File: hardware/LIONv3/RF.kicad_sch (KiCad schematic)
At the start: 17 parts, among them U5 E80-900M2213S, U6 INA226AIDGSR, U7 XL-1608UBC-04, U8 W25Q16JVSSIQTR

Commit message: feat(hardware): annotate schematic with I2C addresses
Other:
- note added: "Table 6-2 (Page 18)"
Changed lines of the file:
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@@
+		)
+	)
+	(text "Table 6-2 (Page 18)"
+		(exclude_from_sim no)
+		(at 143.51 69.85 0)
+		(effects
+			(font
+				(size 1.27 1.27)
+			)
 		)
 	)
@@
 		)
 	)
+	(table
+		(column_count 5)
+		(border
+			(external no)
+			(header yes)
+			(stroke
+				(width 0)
+				(type solid)
+			)
+		)
+		(separators
+			(rows no)
+			(cols no)
+		)
+		(column_widths 5.08 5.08 10.16 6.35 5.08)
+		(row_heights 2.54 2.54)
+		(cells
+			(table_cell "A0"
+				(exclude_from_sim no)
+				(at 127 71.12 0)
+				(size 5.08 2.54)
+				(margins 0.9525 0.9525 0.9525 0.9525)
+				(span 1 1)
+				(fill
+					(type none)
+				)
+				(effects
+					(font
+						(size 1.27 1.27)
+					)
+					(justify left top)
+				)
+			)
+			(table_cell "A1"
+				(exclude_from_sim no)
+				(at 132.08 71.12 0)
+				(size 5.08 2.54)
+				(margins 0.9525 0.9525 0.9525 0.9525)
+				(span 1 1)
+				(fill
+					(type none)
+				)
+				(effects
+					(font
+						(size 1.27 1.27)
+					)
+					(justify left top)
+				)
+			)
+			(table_cell "Binary"
+				(exclude_from_sim no)
+				(at 137.16 71.12 0)
+				(size 10.16 2.54)
+				(margins 0.9525 0.9525 0.9525 0.9525)
+				(span 1 1)
+				(fill
+					(type none)
+				)
+				(effects
+					(font
+						(size 1.27 1.27)
+					)
+					(justify left top)
+				)
+			)
+			(table_cell "Hex"
+				(exclude_from_sim no)
+				(at 147.32 71.12 0)
+				(size 6.35 2.54)
+				(margins 0.9525 0.9525 0.9525 0.9525)
+				(span 1 1)
+				(fill
+					(type none)
+				)
+				(effects
+					(font
+						(size 1.27 1.27)
+					)
+					(justify left top)
+				)
+			)
+			(table_cell "Dec"
+				(exclude_from_sim no)
+				(at 153.67 71.12 0)
+				(size 5.08 2.54)
+				(margins 0.9525 0.9525 0.9525 0.9525)
+				(span 1 1)
+				(fill
+					(type none)
+				)
+				(effects
+					(font
+						(size 1.27 1.27)
+					)
+					(justify left top)
+				)
+			)
+			(table_cell "GND"
+				(exclude_from_sim no)
+				(at 127 73.66 0)
+				(size 5.08 2.54)
+				(margins 0.9525 0.9525 0.9525 0.9525)
+				(span 1 1)
+				(fill
+					(type none)
+				)
+				(effects
+					(font
+						(size 1.27 1.27)
+					)
+					(justify left top)
+				)
+			)
+			(table_cell "GND"
+				(exclude_from_sim no)
+				(at 132.08 73.66 0)
+				(size 5.08 2.54)
+				(margins 0.9525 0.9525 0.9525 0.9525)
+				(span 1 1)
+				(fill
+					(type none)
+				)
+				(effects
+					(font
+						(size 1.27 1.27)
+					)
+					(justify left top)
+				)
+			)
+			(table_cell "1000000"
+				(exclude_from_sim no)
+				(at 137.16 73.66 0)
+				(size 10.16 2.54)
+				(margins 0.9525 0.9525 0.9525 0.9525)
+				(span 1 1)
+				(fill
+					(type none)
+				)
+				(effects
+					(font
+						(size 1.27 1.27)
+					)
+					(justify left top)
+				)
+			)
+			(table_cell "0x40"
+				(exclude_from_sim no)
+				(at 147.32 73.66 0)
+				(size 6.35 2.54)
+				(margins 0.9525 0.9525 0.9525 0.9525)
+				(span 1 1)
+				(fill
+					(type none)
+				)
+				(effects
+					(font
+						(size 1.27 1.27)
+					)
+					(justify left top)
+				)
+			)
+			(table_cell "64"
+				(exclude_from_sim no)
+				(at 153.67 73.66 0)
+				(size 5.08 2.54)
+				(margins 0.9525 0.9525 0.9525 0.9525)
+				(span 1 1)
+				(fill
+					(type none)
+				)
+				(effects
+					(font
+						(size 1.27 1.27)
+					)
+					(justify left top)
+				)
+			)
+		)
+	)

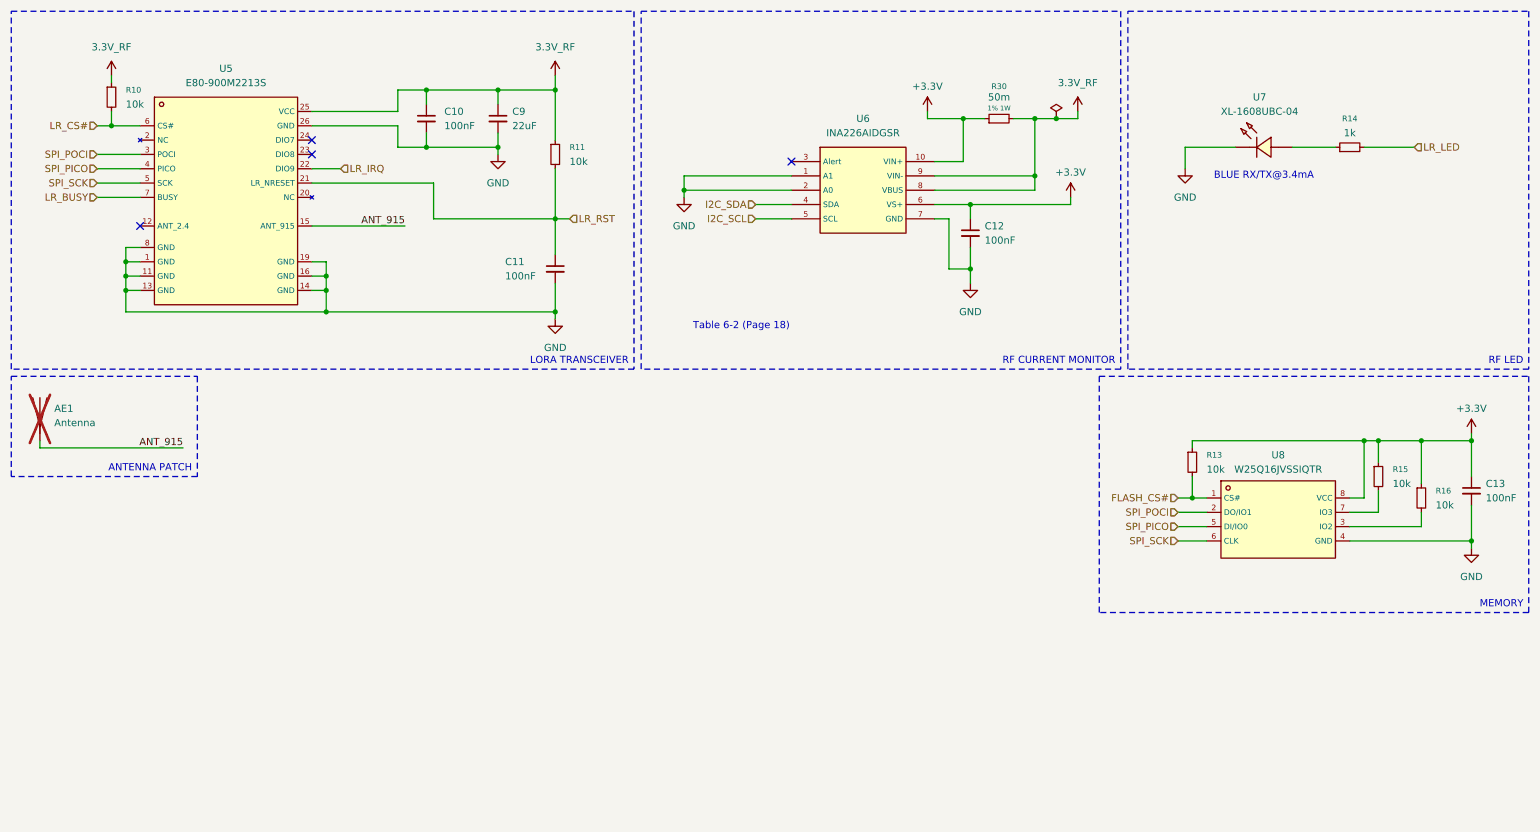
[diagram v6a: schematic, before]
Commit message: refactor(hardware): reorganize schematic
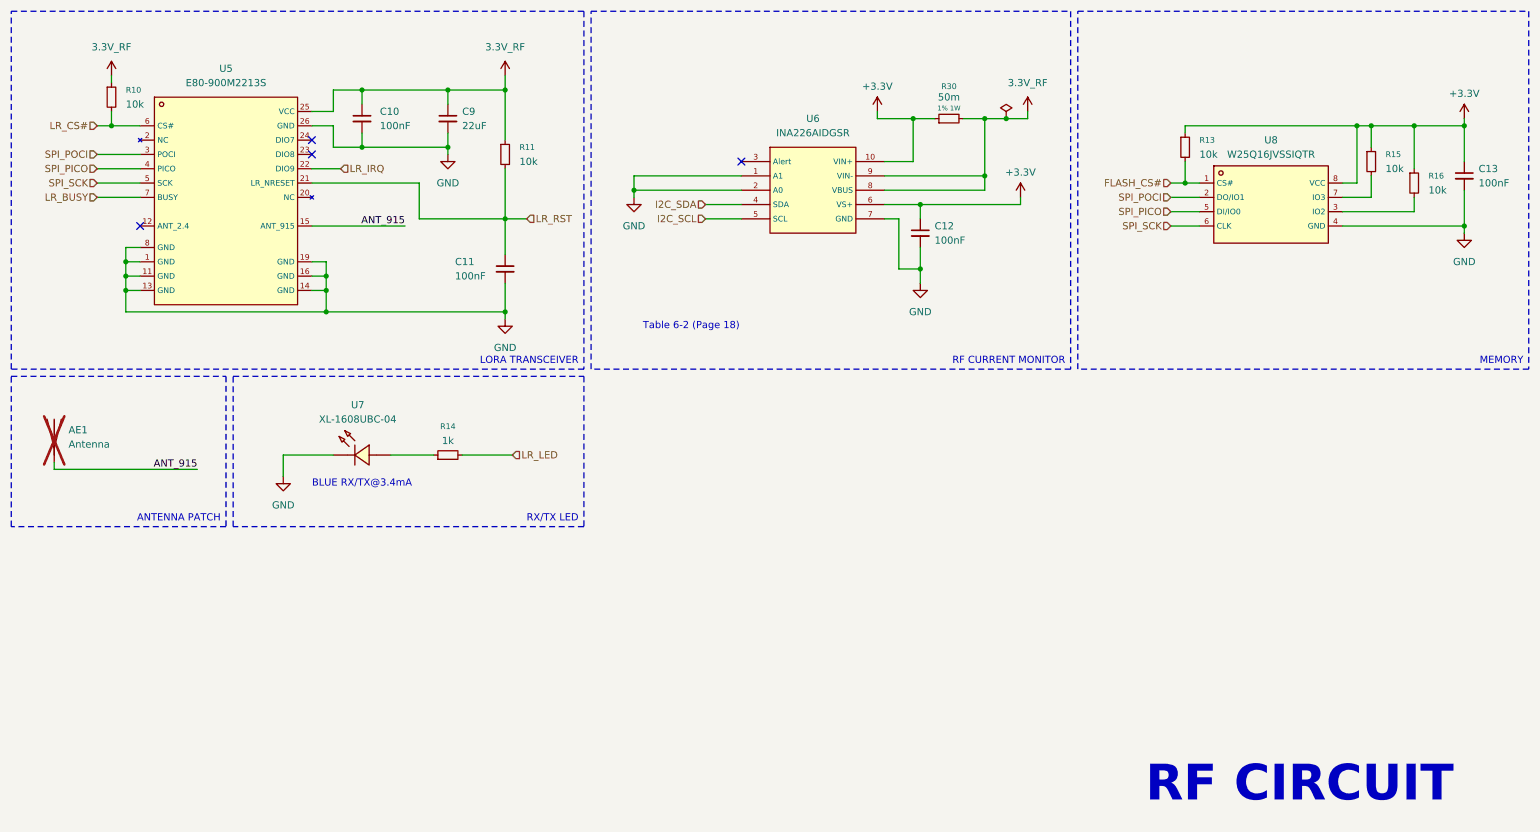
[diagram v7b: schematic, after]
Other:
- note added: "RF CIRCUIT"
- moved on the sheet: AE1, C10, C11, C12, C13, C9, R11, R13, R14, R15, R16, R30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

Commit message: feat(hardware): major schematic improvements
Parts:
- R14: value 1k -> 120
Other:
- note added: "(3.3-3)/120"
- note added: "BLUE RX/TX@3mA"
- note removed: "BLUE RX/TX@3.4mA"
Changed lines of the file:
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@@
 		(comment 3 "2026-08-12")
 	)
-	(text "BLUE RX/TX@3.4mA"
+	(text "BLUE RX/TX@3mA"
 		(exclude_from_sim no)
 		(at 76.2 97.79 0)
@@
 		(exclude_from_sim no)
 		(at 134.62 69.85 0)
+		(effects
+			(font
+				(size 1.27 1.27)
+			)
+		)
+	)
+	(text "(3.3-3)/120"
+		(exclude_from_sim no)
+		(at 76.2 100.33 0)
 		(effects
 			(font
@@
 			)
 		)
-		(property "Value" "1k"
+		(property "Value" "120"
 			(at 91.44 90.17 90)
 			(show_name no)
